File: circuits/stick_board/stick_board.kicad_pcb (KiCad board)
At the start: 2 copper layers, 129.2 x 51.2 mm, 22 parts, among them J1 Conn_01x13_Pin, M1 Motor_DC, M2 Motor_DC, Q1 AO3400A, Q2 AO3400A, U1 GULI, U2 GULI, U3 DRV5055A1xDBZxQ1, U4 DRV5055A1xDBZxQ1

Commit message: 优化stick板边缘
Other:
- board size 129.2 x 51.2 mm -> 129.2 x 50.9 mm
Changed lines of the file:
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@@
     )
   )
+  (gr_line (start 198.35 99.14) (end 198.83 100.16)
+    (stroke (width 0.1) (type default)) (layer "Edge.Cuts"))
   (gr_line (start 205.7 134.875) (end 205.7 131.55)
     (stroke (width 0.1) (type default)) (layer "Edge.Cuts"))
   (gr_line (start 82.475 136.525) (end 76.5 134.875)
     (stroke (width 0.1) (type default)) (layer "Edge.Cuts"))
-  (gr_circle (center 195.325 133.6) (end 196.575 133.6)
+  (gr_line (start 83.49 100.31) (end 84.31 99.08)
+    (stroke (width 0.1) (type default)) (layer "Edge.Cuts"))
+  (gr_circle (center 195.325 133.6) (end 196.625 133.6)
     (stroke (width 0.1) (type default)) (fill none) (layer "Edge.Cuts"))
   (gr_line (start 179.3 147.2) (end 179.3 142)
@@
   (gr_line (start 111.7 122.3) (end 170.5 122.3)
     (stroke (width 0.1) (type default)) (layer "Edge.Cuts"))
+  (gr_line (start 196.19 98.21) (end 197.59 98.45)
+    (stroke (width 0.1) (type default)) (layer "Edge.Cuts"))
+  (gr_line (start 194.59 98.59) (end 196.19 98.21)
+    (stroke (width 0.1) (type default)) (layer "Edge.Cuts"))
   (gr_line (start 90.975 138.925) (end 90.775 137.725)
     (stroke (width 0.1) (type default)) (layer "Edge.Cuts"))
-  (gr_circle (center 86.875 133.6) (end 88.125 133.6)
+  (gr_circle (center 86.875 133.6) (end 88.175 133.6)
     (stroke (width 0.1) (type default)) (fill none) (layer "Edge.Cuts"))
   (gr_line (start 76.5 134.875) (end 76.5 131.55)
     (stroke (width 0.1) (type default)) (layer "Edge.Cuts"))
-  (gr_line (start 194.9 97.9) (end 197.64 97.9)
-    (stroke (width 0.1) (type default)) (layer "Edge.Cuts"))
   (gr_line (start 102.9 147.2) (end 102.9 142)
     (stroke (width 0.1) (type default)) (layer "Edge.Cuts"))
-  (gr_line (start 193 100.50868) (end 194.9 97.9)
+  (gr_line (start 193 100.50868) (end 194.59 98.59)
     (stroke (width 0.1) (type default)) (layer "Edge.Cuts"))
-  (gr_line (start 83.314672 99.555654) (end 83.329344 102.89132)
+  (gr_line (start 83.49 100.31) (end 83.329344 102.89132)
     (stroke (width 0.1) (type default)) (layer "Edge.Cuts"))
   (gr_line (start 191.225 138.925) (end 191.425 137.725)
@@
   (gr_line (start 191.425 137.725) (end 198.85 135.8)
     (stroke (width 0.1) (type default)) (layer "Edge.Cuts"))
-  (gr_line (start 83.314672 99.555654) (end 84.9 97.89132)
+  (gr_line (start 86.74 98.48) (end 87.67 98.71)
     (stroke (width 0.1) (type default)) (layer "Edge.Cuts"))
   (gr_line (start 78.1 125.25) (end 83.329344 102.89132)
@@
   (gr_line (start 111.7 100.5) (end 89.3 100.5)
     (stroke (width 0.1) (type default)) (layer "Edge.Cuts"))
-  (gr_line (start 87.4 97.89132) (end 89.3 100.5)
+  (gr_line (start 87.67 98.71) (end 89.3 100.5)
     (stroke (width 0.1) (type default)) (layer "Edge.Cuts"))
   (gr_line (start 170.5 122.3) (end 170.5 100.5)
     (stroke (width 0.1) (type default)) (layer "Edge.Cuts"))
-  (gr_line (start 87.4 97.89132) (end 84.9 97.89132)
-    (stroke (width 0.1) (type default)) (layer "Edge.Cuts"))
   (gr_circle (center 78.75 132.8) (end 80 132.8)
     (stroke (width 0.1) (type default)) (fill none) (layer "Edge.Cuts"))
+  (gr_line (start 85.47 98.53) (end 86.74 98.48)
+    (stroke (width 0.1) (type default)) (layer "Edge.Cuts"))
   (gr_line (start 104.4 149.1) (end 177.8 149.1)
     (stroke (width 0.1) (type default)) (layer "Edge.Cuts"))
   (gr_circle (center 196.2 101) (end 197.75 101)
     (stroke (width 0.1) (type default)) (fill none) (layer "Edge.Cuts"))
+  (gr_line (start 197.59 98.45) (end 198.35 99.14)
+    (stroke (width 0.1) (type default)) (layer "Edge.Cuts"))
   (gr_circle (center 203.45 132.8) (end 204.7 132.8)
     (stroke (width 0.1) (type default)) (fill none) (layer "Edge.Cuts"))
@@
   (gr_line (start 198.85 135.8) (end 199.725 136.525)
     (stroke (width 0.1) (type default)) (layer "Edge.Cuts"))
-  (gr_line (start 199 102.9) (end 198.985328 99.564334)
+  (gr_line (start 199 102.9) (end 198.83 100.16)
     (stroke (width 0.1) (type default)) (layer "Edge.Cuts"))
   (gr_line (start 102.9 142) (end 90.975 138.925)
     (stroke (width 0.1) (type default)) (layer "Edge.Cuts"))
-  (gr_line (start 197.64 97.9) (end 198.985328 99.564334)
+  (gr_line (start 84.31 99.08) (end 85.47 98.53)
     (stroke (width 0.1) (type default)) (layer "Edge.Cuts"))
   (segment (start 104.2 118.8) (end 104.2 117.3) (width 0.5) (layer "F.Cu") (net 1))

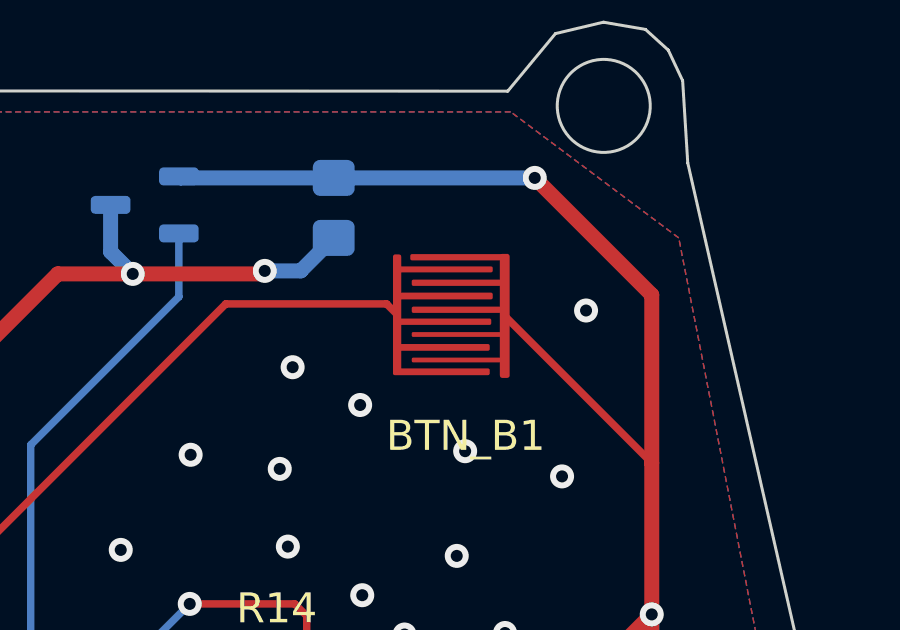
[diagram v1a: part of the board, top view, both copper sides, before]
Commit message: 更新stick板按键封装
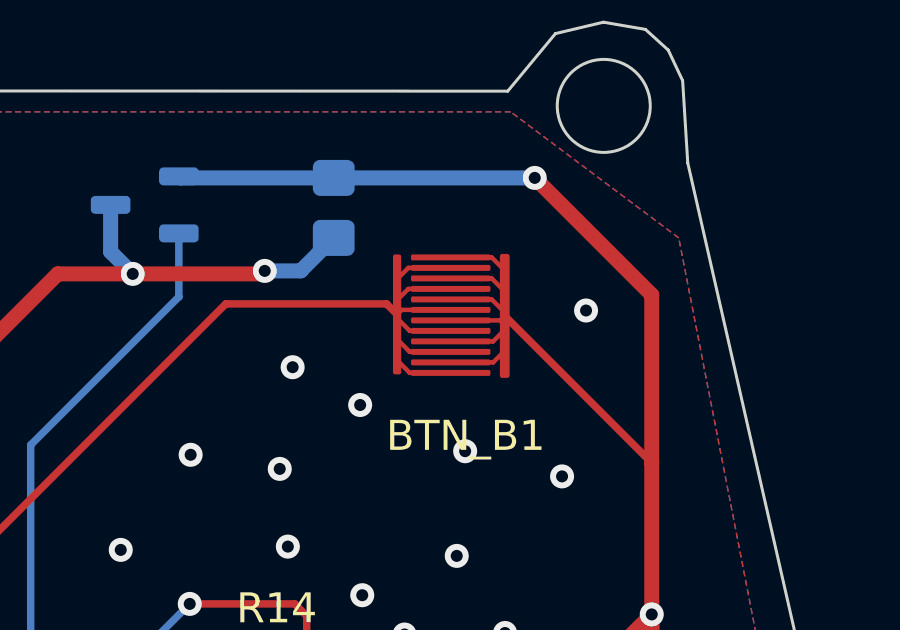
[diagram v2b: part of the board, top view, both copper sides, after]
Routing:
- net +3V3: track 281.9 -> 298.9 mm
- net /BTN_B: track 84.8 -> 101.7 mm

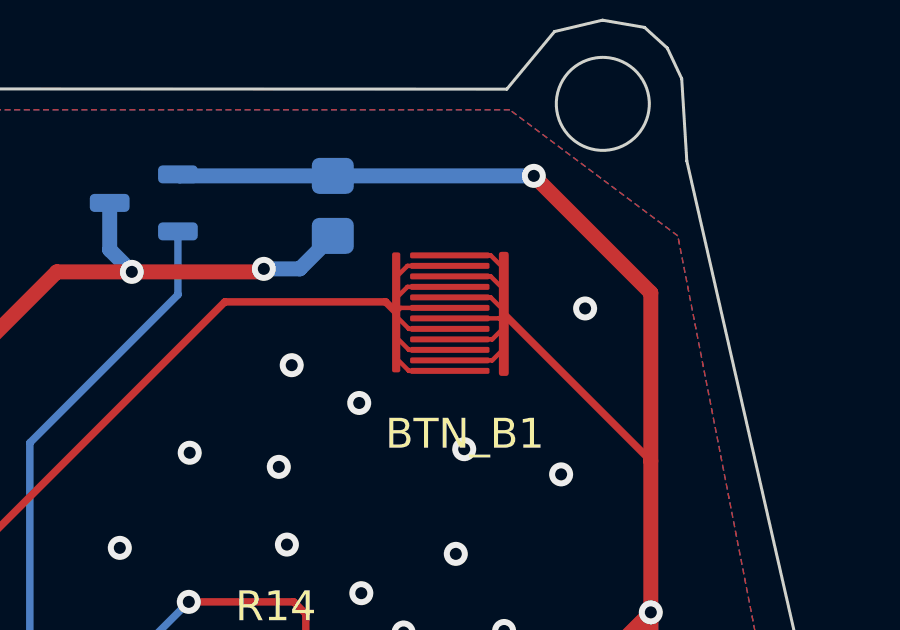
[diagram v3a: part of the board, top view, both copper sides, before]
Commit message: 更新摇杆板触摸键封装
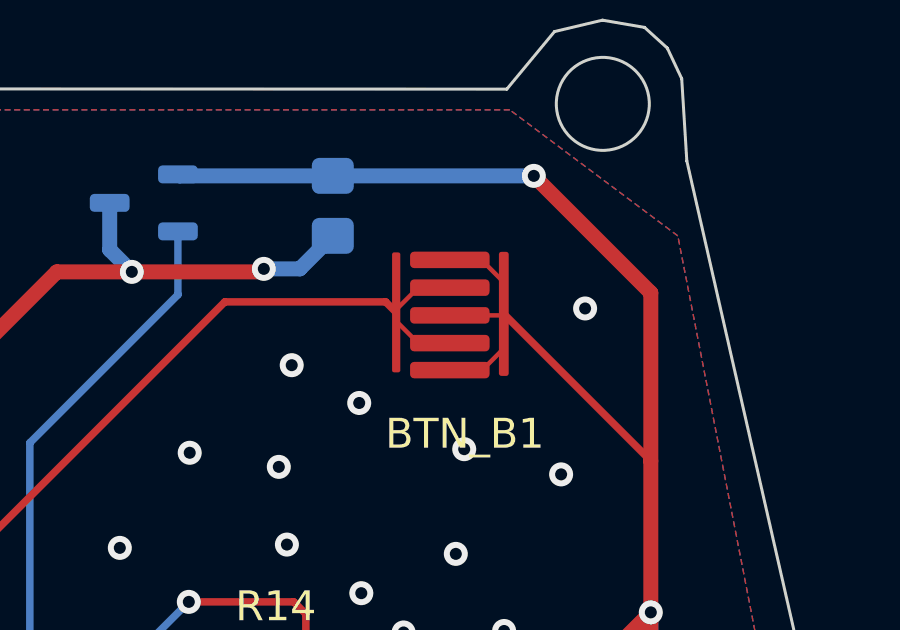
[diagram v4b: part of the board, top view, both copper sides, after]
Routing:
- net /BTN_B: track 101.7 -> 94.6 mm
- net +3V3: track 298.9 -> 294.0 mm

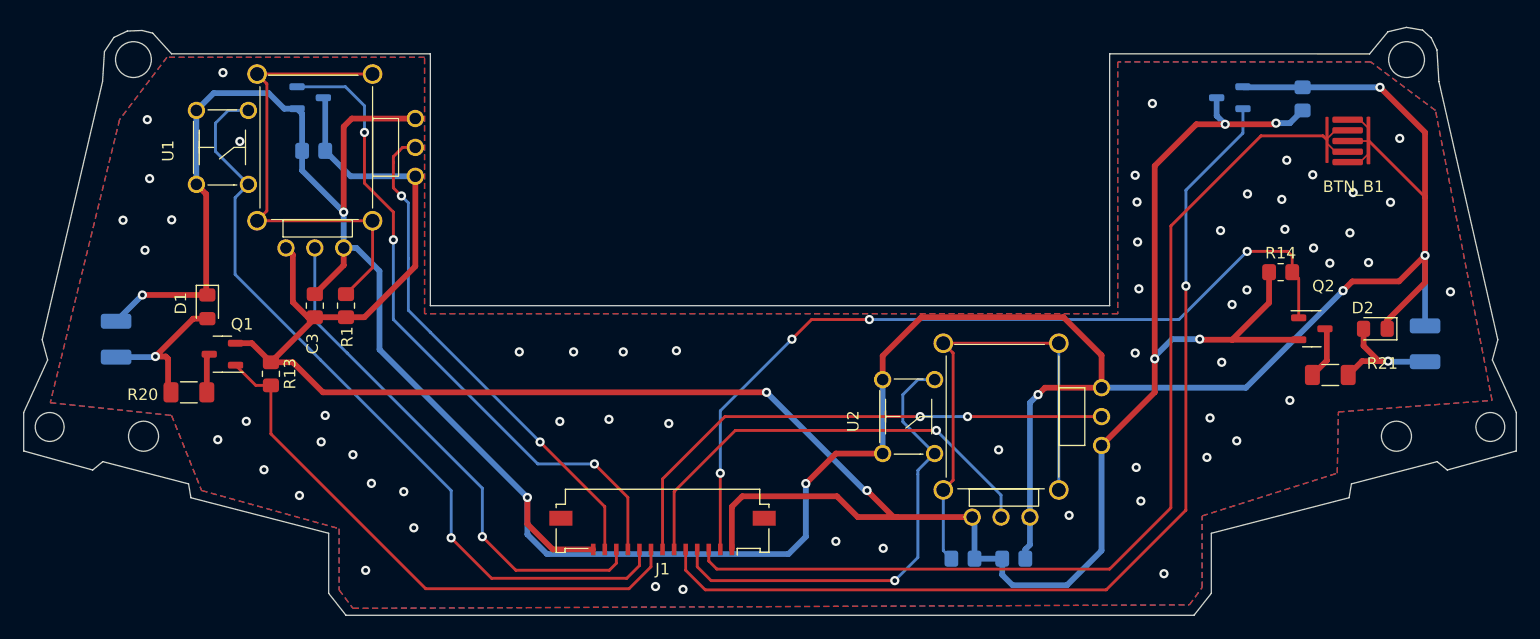
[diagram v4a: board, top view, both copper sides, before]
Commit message: 马达驱动增加栅极电阻
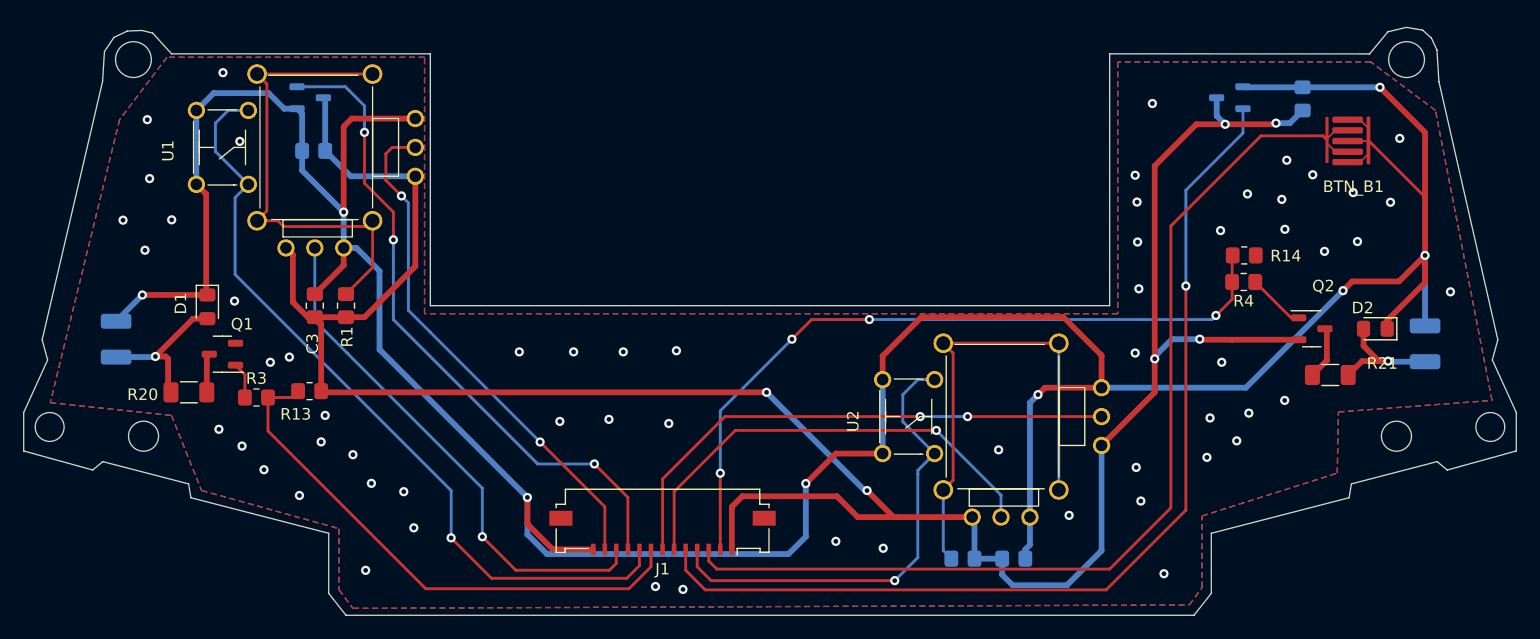
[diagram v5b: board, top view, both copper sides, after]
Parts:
- added R3: 1K, Resistor_SMD:R_0805_2012Metric_Pad1.20x1.40mm_HandSolder, F.Cu at (96.7, 130.2)
- added R4: 1K, Resistor_SMD:R_0805_2012Metric_Pad1.20x1.40mm_HandSolder, F.Cu at (182.1, 120.2)
- moved R13 3.67 mm to (101.2, 129.7), turned to 180 degrees
- moved R14 3.47 mm to (182.2, 118.0), turned to 180 degrees
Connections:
- Q1 pad 1: /MOTOR1 -> Net-(Q1-G)
- Q2 pad 1: /MOTOR2 -> Net-(Q2-G)
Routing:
- net GND: track 224.6 -> 209.4 mm
- net /MOTOR2: track 73.0 -> 64.1 mm
- net Net-(Q2-G): track 0.00 -> 5.05 mm
- net Net-(Q1-G): track 0.00 -> 3.14 mm
- net /MOTOR1: track 48.7 -> 46.8 mm
- net /LEFT_X: track 43.8 -> 44.9 mm

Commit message: 差手柄机械按键位置
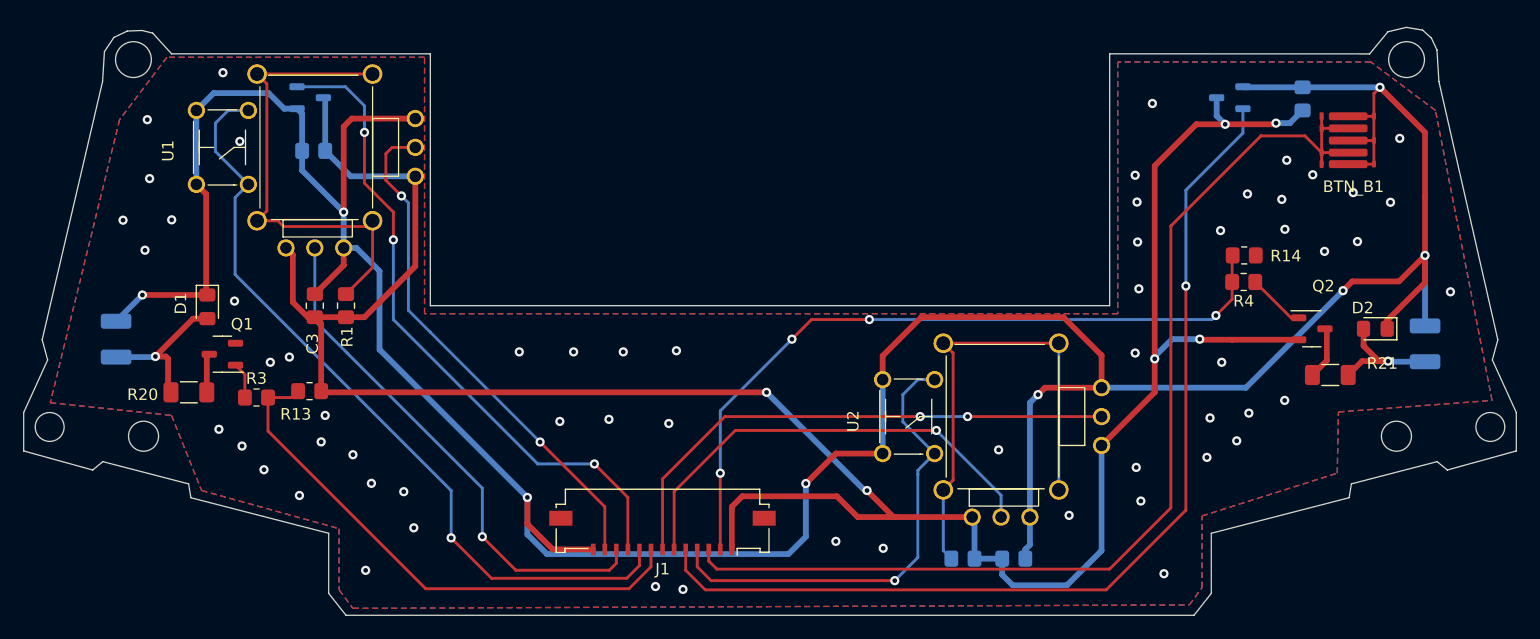
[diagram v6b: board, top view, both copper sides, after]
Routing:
- net +3V3: track 294.0 -> 288.5 mm
- net /BTN_B: track 94.6 -> 93.5 mm

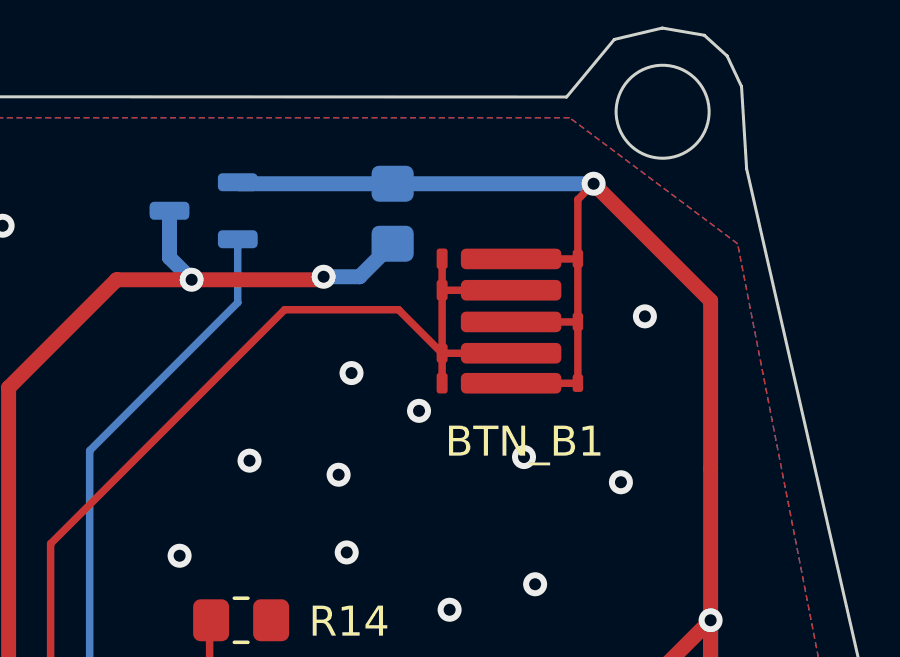
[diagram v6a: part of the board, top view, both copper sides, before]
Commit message: 调整封装,待打样测试
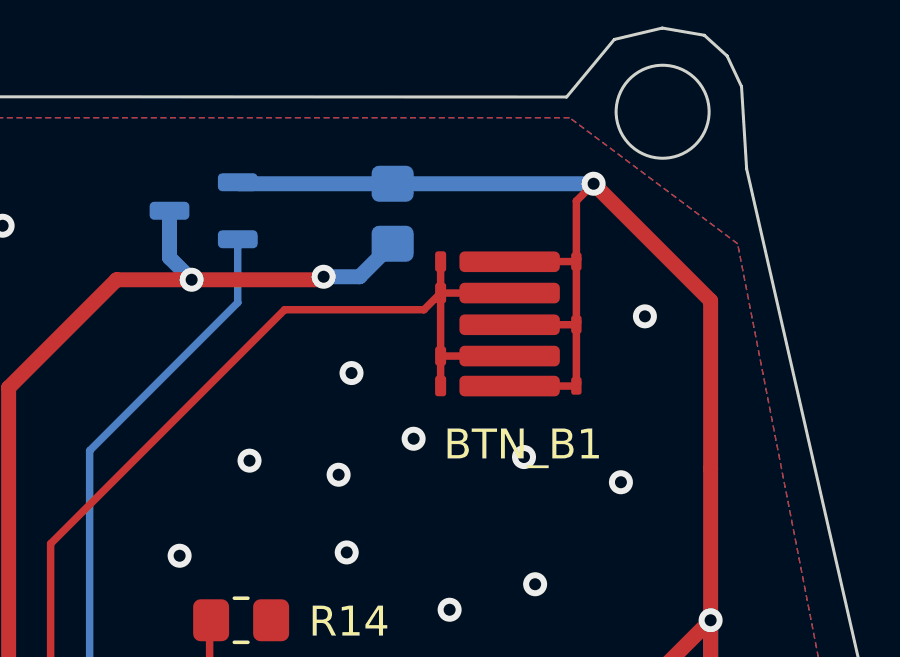
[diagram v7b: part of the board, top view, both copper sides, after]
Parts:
- moved BTN_B1 0.11 mm to (191.2, 108.1)

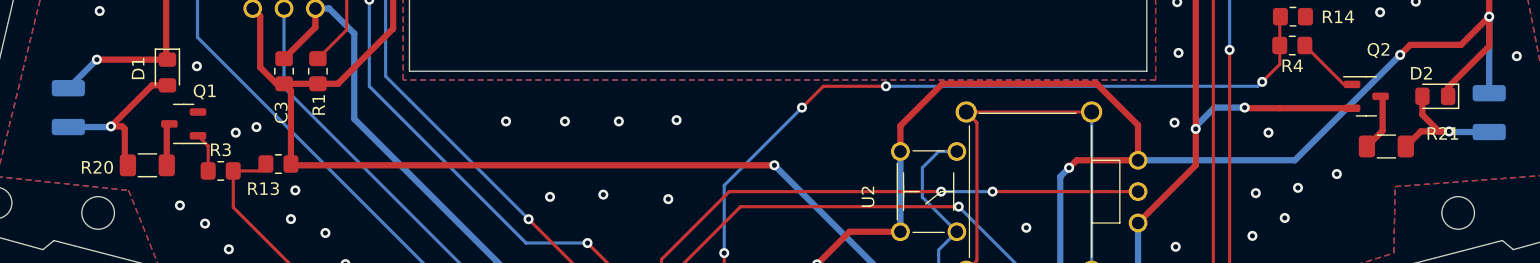
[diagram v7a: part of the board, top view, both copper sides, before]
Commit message: stick板去除马达限流电阻
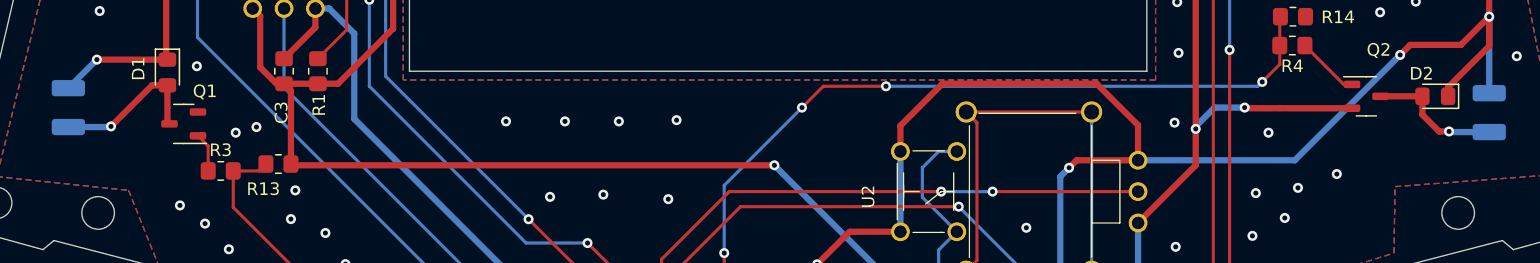
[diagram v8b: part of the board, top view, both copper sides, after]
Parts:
- removed R20, R21: 10R, Resistor_SMD:R_1206_3216Metric_Pad1.30x1.75mm_HandSolder
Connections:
- Q1 pad 3: Net-(Q1-D) -> Net-(D1-A)
- Q2 pad 3: Net-(Q2-D) -> Net-(D2-A)
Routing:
- net Net-(Q2-D): track 4.59 -> 0.00 mm
- net Net-(Q1-D): track 3.62 -> 0.00 mm
- net Net-(D1-A): track 13.5 -> 12.4 mm
